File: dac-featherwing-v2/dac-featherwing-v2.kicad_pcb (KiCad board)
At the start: 2 copper layers, 22.9 x 50.7 mm, 15 parts, among them J1 BOT, J2 TOP, J3 35RASMT4BHNTRX, U1 WM1824CGEFL, U2 TLV320AIC3104IRHBR

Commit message: Dac featherwing schematic v2
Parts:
- removed U2: TLV320AIC3104IRHBR, Footprints:IC_ADS125H01IRHBT

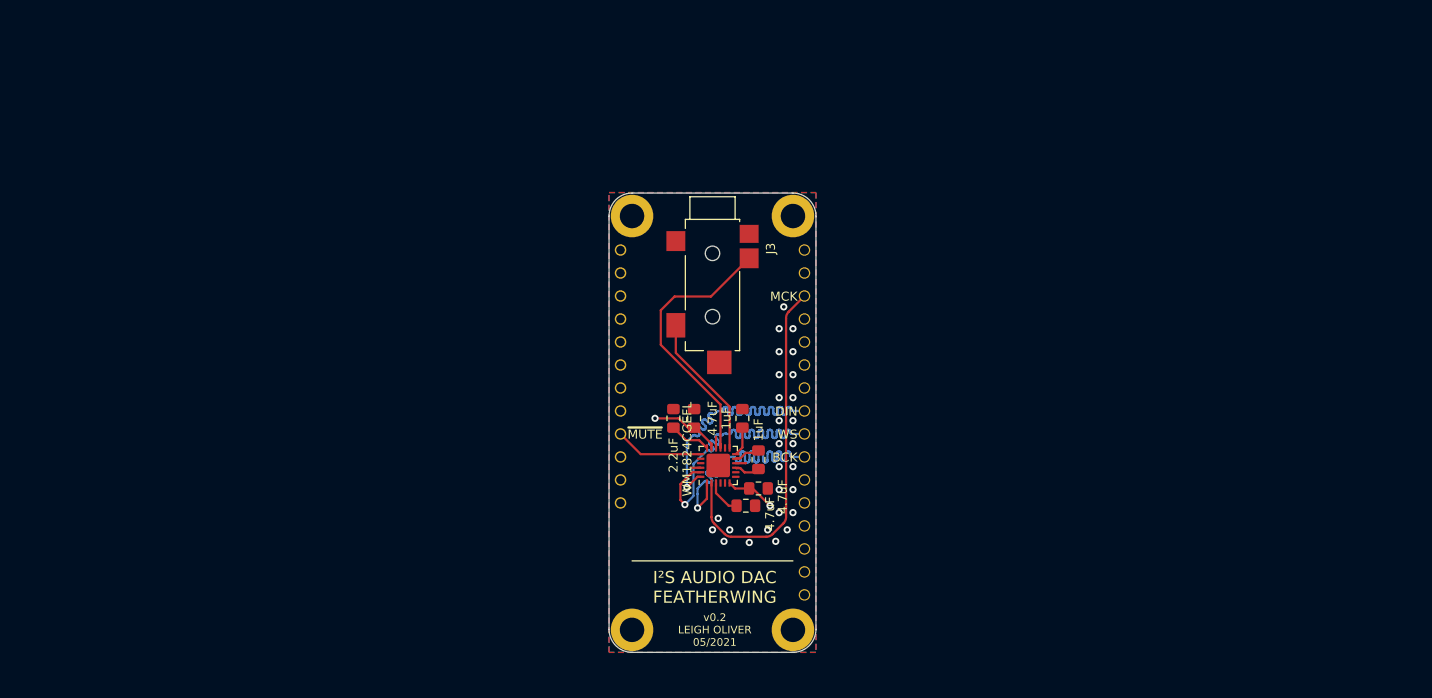
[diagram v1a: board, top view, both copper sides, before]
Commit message: Work on DAC Featherwing v2
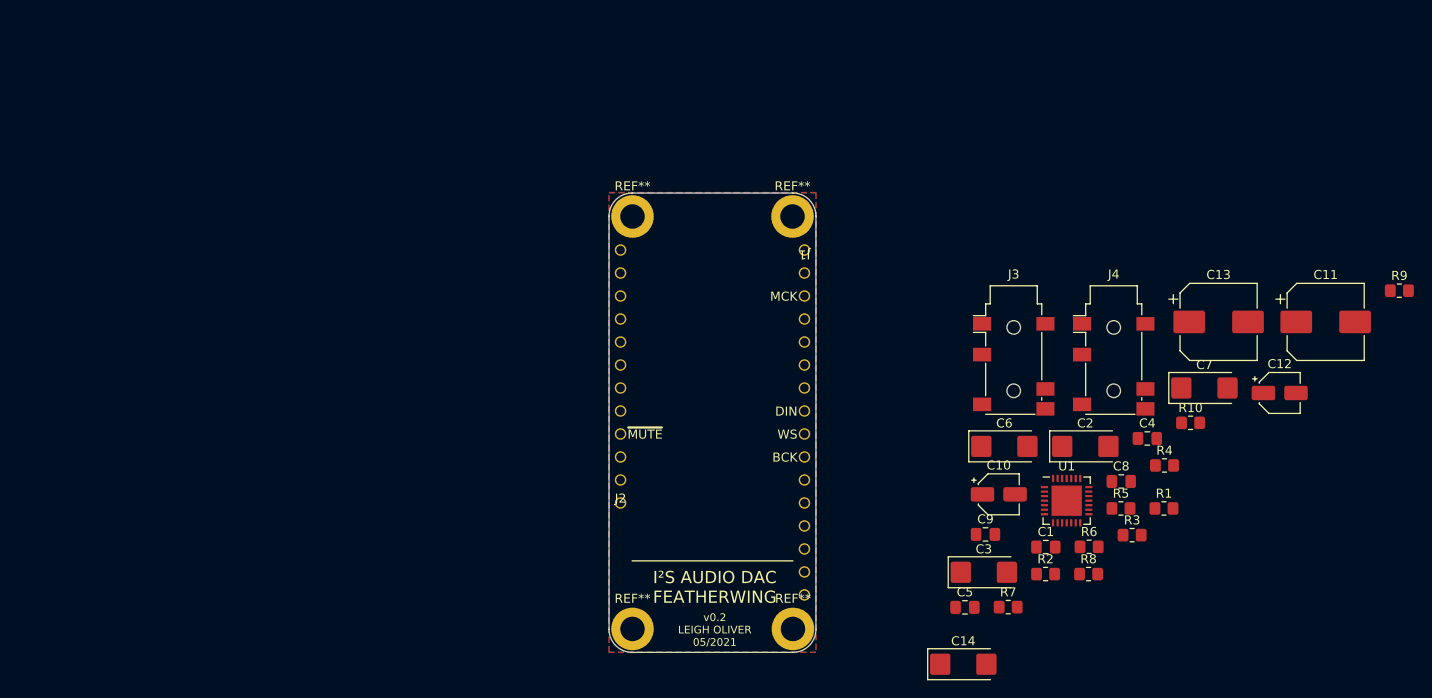
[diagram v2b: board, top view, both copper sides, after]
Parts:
- removed the REF** at (157.5, 75.2)
- removed the REF** at (175.3, 120.9)
- removed the REF** at (157.5, 120.9)
- removed the REF** at (175.3, 75.2)
- added C10: 1uF, Capacitor_SMD:CP_Elec_4x4.5, F.Cu at (198.0, 105.9)
- added C11: 220uF, Capacitor_SMD:CP_Elec_8x10, F.Cu at (234.1, 86.9)
- added C12: 1uF, Capacitor_SMD:CP_Elec_4x4.5, F.Cu at (229.0, 94.7)
- added C13: 220uF, Capacitor_SMD:CP_Elec_8x10, F.Cu at (222.3, 86.9)
- added C14: 10uF, Capacitor_Tantalum_SMD:CP_EIA-6032-20_AVX-F_Pad2.25x2.35mm_HandSolder, F.Cu at (194.1, 124.7)
- added C7: 10uF, Capacitor_Tantalum_SMD:CP_EIA-6032-20_AVX-F_Pad2.25x2.35mm_HandSolder, F.Cu at (220.7, 94.2)
- added C8: 0.1uF, Capacitor_SMD:C_0805_2012Metric_Pad1.18x1.45mm_HandSolder, F.Cu at (211.5, 104.5)
- added C9: 0.1uF, Capacitor_SMD:C_0805_2012Metric_Pad1.18x1.45mm_HandSolder, F.Cu at (196.5, 110.4)
- added J4: AudioJack4, Connector_Audio:Jack_3.5mm_PJ311_Horizontal, F.Cu at (210.7, 91.8)
- added R1: 4.7K, Resistor_SMD:R_0805_2012Metric_Pad1.20x1.40mm_HandSolder, F.Cu at (216.2, 107.5)
- added R10: 100, Resistor_SMD:R_0805_2012Metric_Pad1.20x1.40mm_HandSolder, F.Cu at (219.2, 98.0)
- added R2: 4.7K, Resistor_SMD:R_0805_2012Metric_Pad1.20x1.40mm_HandSolder, F.Cu at (203.2, 114.7)
- added R3: 10K, Resistor_SMD:R_0805_2012Metric_Pad1.20x1.40mm_HandSolder, F.Cu at (212.7, 110.4)
- added R4: 100, Resistor_SMD:R_0805_2012Metric_Pad1.20x1.40mm_HandSolder, F.Cu at (216.3, 102.7)
- added R5: 47K, Resistor_SMD:R_0805_2012Metric_Pad1.20x1.40mm_HandSolder, F.Cu at (211.5, 107.5)
- added R6: 47K, Resistor_SMD:R_0805_2012Metric_Pad1.20x1.40mm_HandSolder, F.Cu at (208.0, 111.7)
- added R7: 47K, Resistor_SMD:R_0805_2012Metric_Pad1.20x1.40mm_HandSolder, F.Cu at (199.0, 118.4)
- added R8: 47K, Resistor_SMD:R_0805_2012Metric_Pad1.20x1.40mm_HandSolder, F.Cu at (207.9, 114.7)
- added R9: 100, Resistor_SMD:R_0805_2012Metric_Pad1.20x1.40mm_HandSolder, F.Cu at (242.3, 83.4)
- added REF**: MountingHole_2.7mm_M2.5_DIN965_Pad, MountingHole:MountingHole_2.7mm_M2.5_DIN965_Pad, F.Cu at (157.5, 75.2)
- added REF**: MountingHole_2.7mm_M2.5_DIN965_Pad, MountingHole:MountingHole_2.7mm_M2.5_DIN965_Pad, F.Cu at (175.2, 75.2)
- added REF**: MountingHole_2.7mm_M2.5_DIN965_Pad, MountingHole:MountingHole_2.7mm_M2.5_DIN965_Pad, F.Cu at (157.5, 120.8)
- added REF**: MountingHole_2.7mm_M2.5_DIN965_Pad, MountingHole:MountingHole_2.7mm_M2.5_DIN965_Pad, F.Cu at (175.3, 120.8)
- C1, C5: value 4.7uF -> 0.1uF; footprint Capacitor_SMD:C_0805_2012Metric_Pad1.15x1.40mm_HandSolder -> Capacitor_SMD:C_0805_2012Metric_Pad1.18x1.45mm_HandSolder
- C2: value 4.7uF -> 10uF; footprint Capacitor_SMD:C_0805_2012Metric_Pad1.15x1.40mm_HandSolder -> Capacitor_Tantalum_SMD:CP_EIA-6032-20_AVX-F_Pad2.25x2.35mm_HandSolder
- C3: value 1uF -> 10uF; footprint Capacitor_SMD:C_0805_2012Metric_Pad1.15x1.40mm_HandSolder -> Capacitor_Tantalum_SMD:CP_EIA-6032-20_AVX-F_Pad2.25x2.35mm_HandSolder
- C4: value 1uF -> 0.1uF; footprint Capacitor_SMD:C_0805_2012Metric_Pad1.15x1.40mm_HandSolder -> Capacitor_SMD:C_0805_2012Metric_Pad1.18x1.45mm_HandSolder
- C6: value 2.2uF -> 10uF; footprint Capacitor_SMD:C_0805_2012Metric_Pad1.15x1.40mm_HandSolder -> Capacitor_Tantalum_SMD:CP_EIA-6032-20_AVX-F_Pad2.25x2.35mm_HandSolder
- J3: value 35RASMT4BHNTRX -> AudioJack4; footprint Footprints:SWITCHCRAFT_35RASMT4BHNTRX -> Connector_Audio:Jack_3.5mm_PJ311_Horizontal
- U1: value WM1824CGEFL -> WM8731CLSEFL; footprint Package_DFN_QFN:QFN-24-1EP_4x4mm_P0.5mm_EP2.6x2.6mm -> Package_DFN_QFN:QFN-28-1EP_5x5mm_P0.5mm_EP3.35x3.35mm
- moved C4 44.8 mm to (214.4, 99.8), turned to 0 degrees
- moved U1 38.7 mm to (205.5, 106.6), turned to 0 degrees
- moved C6 36.7 mm to (198.6, 100.6), turned to 0 degrees
- moved C5 36.5 mm to (194.3, 118.4), turned to 0 degrees
- moved C2 36.4 mm to (207.6, 100.6)
- moved J3 34.5 mm to (199.7, 91.8), turned to 0 degrees
- moved C1 33.5 mm to (203.2, 111.8)
- moved C3 27.8 mm to (196.3, 114.5), turned to 0 degrees
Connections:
- C1 pad 1: Net-(C1-Pad1) -> +3V3
- C3 pad 1: Net-(C3-Pad1) -> +3V3
- C3 pad 2: Net-(C3-Pad2) -> GND
- C4 pad 1: Net-(C4-Pad1) -> +3V3
- C5 pad 1: +3V3 -> +3.3VA
- C6 pad 1: Net-(C6-Pad1) -> +3.3VA
- J1 pad 3: /U1RXD/CLK_OUT3 -> /I2S_MCLK
- J3 pad 1: GND -> (no net)
- J3 pad 2: /OUTL -> (no net)
- J3 pad 3: /OUTR -> (no net)
- J3 pad 4: unconnected-(J3-Pad4) -> (no net)
- J3 pad 5: unconnected-(J3-Pad5) -> (no net)
- U1 pad 1: /I2S_BCK -> /I2S_MCLK
- U1 pad 10: GND -> unconnected-(U1-Pad10)
- U1 pad 11: Net-(C3-Pad2) -> unconnected-(U1-Pad11)
- U1 pad 12: Net-(C4-Pad1) -> +3.3VA
- U1 pad 13: /OUTR -> Net-(C11-Pad1)
- U1 pad 14: unconnected-(U1-Pad14) -> Net-(C13-Pad1)
- U1 pad 15: /OUTL -> GND
- U1 pad 16: GND -> Net-(C10-Pad1)
- U1 pad 17: +3V3 -> Net-(C12-Pad1)
- U1 pad 18: Net-(C6-Pad1) -> +3.3VA
- U1 pad 19: /~MUTE -> GND
- U1 pad 20: unconnected-(U1-Pad20) -> Net-(C14-Pad1)
- U1 pad 22: GND -> unconnected-(U1-Pad22)
- U1 pad 23: /I2S_WS -> unconnected-(U1-Pad23)
- U1 pad 24: /I2S_DO -> unconnected-(U1-Pad24)
- U1 pad 25: (no net) -> Net-(R3-Pad1)
- U1 pad 3: Net-(C1-Pad1) -> +3V3
- U1 pad 4: unconnected-(U1-Pad4) -> GND
- U1 pad 5: unconnected-(U1-Pad5) -> +3V3
- U1 pad 6: +3V3 -> Net-(R4-Pad2)
- U1 pad 7: unconnected-(U1-Pad7) -> /I2S_BCK
- U1 pad 8: unconnected-(U1-Pad8) -> /I2S_DO
- U1 pad 9: Net-(C3-Pad1) -> /I2S_WS
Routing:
- net unconnected-(U1-Pad2): track 39.3 -> 0.00 mm
- net /I2S_DO: track 35.5 -> 0.00 mm, vias 1 -> 0
- net /I2S_WS: track 35.4 -> 0.00 mm, vias 1 -> 0
- net /I2S_BCK: track 35.4 -> 0.00 mm, vias 1 -> 0
- net /OUTL: track 30.5 -> 0.00 mm
- net /OUTR: track 16.0 -> 0.00 mm
- net +3V3: track 13.4 -> 0.00 mm, vias 2 -> 0
- net /~MUTE: track 9.78 -> 0.00 mm
- net Net-(C6-Pad1): track 4.63 -> 0.00 mm
- net Net-(C1-Pad1): track 3.96 -> 0.00 mm
- net GND: track 3.47 -> 0.00 mm, vias 28 -> 0
- net Net-(C4-Pad1): track 3.23 -> 0.00 mm
- net Net-(C3-Pad2): track 2.88 -> 0.00 mm
- net Net-(C3-Pad1): track 2.87 -> 0.00 mm

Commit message: Capacitors checked. TRRS pins checked. 3.5mm Footprint made. Performing layout and routing.
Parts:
- removed R4: 100, Resistor_SMD:R_0805_2012Metric_Pad1.20x1.40mm_HandSolder
- removed the REF** at (157.5, 75.2)
- removed the REF** at (175.2, 75.2)
- removed the REF** at (157.5, 120.8)
- removed the REF** at (175.3, 120.8)
- added REF**: MountingHole_2.7mm_M2.5_DIN965_Pad, MountingHole:MountingHole_2.7mm_M2.5_DIN965_Pad, F.Cu at (132.1, 109.2)
- added REF**: MountingHole_2.7mm_M2.5_DIN965_Pad, MountingHole:MountingHole_2.7mm_M2.5_DIN965_Pad, F.Cu at (92.7, 55.9)
- added REF**: MountingHole_2.7mm_M2.5_DIN965_Pad, MountingHole:MountingHole_2.7mm_M2.5_DIN965_Pad, F.Cu at (132.1, 55.9)
- added REF**: MountingHole_2.7mm_M2.5_DIN965_Pad, MountingHole:MountingHole_2.7mm_M2.5_DIN965_Pad, F.Cu at (132.1, 63.5)
- added REF**: MountingHole_2.7mm_M2.5_DIN965_Pad, MountingHole:MountingHole_2.7mm_M2.5_DIN965_Pad, F.Cu at (92.7, 109.2)
- added REF**: MountingHole_2.7mm_M2.5_DIN965_Pad, MountingHole:MountingHole_2.7mm_M2.5_DIN965_Pad, F.Cu at (114.3, 109.2)
- added REF**: MountingHole_2.7mm_M2.5_DIN965_Pad, MountingHole:MountingHole_2.7mm_M2.5_DIN965_Pad, F.Cu at (114.3, 63.5)
- added REF**: MountingHole_2.7mm_M2.5_DIN965_Pad, MountingHole:MountingHole_2.7mm_M2.5_DIN965_Pad, F.Cu at (114.3, 55.9)
- C2, C3: footprint Capacitor_Tantalum_SMD:CP_EIA-6032-20_AVX-F_Pad2.25x2.35mm_HandSolder -> Capacitor_SMD:C_0805_2012Metric_Pad1.18x1.45mm_HandSolder
- C5, C6, C7, C8, R1, R2, R3: moved to B.Cu
- J3, J4: footprint Connector_Audio:Jack_3.5mm_PJ311_Horizontal -> Footprints:Lumberg 1503 20 VP3
- moved C11 138.3 mm to (95.9, 84.2), turned to 90 degrees
- moved R9 122.0 mm to (120.7, 73.8), turned to 90 degrees
- moved R5 118.4 mm to (97.4, 75.9), turned to 180 degrees
- moved C13 116.3 mm to (106.0, 84.2), turned to 90 degrees
- moved R6 109.6 mm to (104.4, 75.9), turned to 180 degrees
- moved C12 103.2 mm to (127.0, 79.5), turned to 90 degrees
- moved J3 101.8 mm to (101.0, 66.8), turned to 90 degrees
- moved C7 96.8 mm to (124.0, 91.9)
- moved R10 96.6 mm to (125.7, 73.8), turned to 90 degrees
- moved R7 94.1 mm to (116.2, 73.8), turned to -90 degrees
- moved J4 91.0 mm to (123.2, 66.8), turned to 90 degrees
- moved C8 88.1 mm to (124.0, 95.0)
- moved R8 87.9 mm to (130.2, 73.8), turned to 90 degrees
- moved R1 87.9 mm to (128.5, 102.6), turned to 180 degrees
- moved R3 86.0 mm to (127.5, 99.1), turned to 90 degrees
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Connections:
- C11 pad 2: LHPOUT -> RHPOUT
- C13 pad 2: RHPOUT -> LHPOUT
- R5 pad 2: LHPOUT -> RHPOUT
- R6 pad 1: RHPOUT -> LHPOUT
- U1 pad 13: Net-(C11-Pad1) -> Net-(C13-Pad1)
- U1 pad 14: Net-(C13-Pad1) -> Net-(C11-Pad1)
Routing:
- net Net-(C11-Pad1): track 0.00 -> 36.1 mm
- net RHPOUT: track 0.00 -> 27.4 mm
- net Net-(C13-Pad1): track 0.00 -> 25.5 mm
- net /I2S_DO: track 0.00 -> 23.0 mm
- net /I2S_WS: track 0.00 -> 22.9 mm
- net /I2S_BCK: track 0.00 -> 22.8 mm
- net LHPOUT: track 0.00 -> 19.0 mm
- net ROUT: track 0.00 -> 12.6 mm
- net Net-(C10-Pad2): track 0.00 -> 7.89 mm
- net Net-(C12-Pad2): track 0.00 -> 7.89 mm
- net LOUT: track 0.00 -> 5.29 mm
- added copper zone on B.Cu, net +3.3VA
- added copper zone on B.Cu, net GND
- removed copper zone on B.Cu, net +3V3
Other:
- board size 22.9 x 50.7 mm -> 44.5 x 58.4 mm
- board text added: "+BAT"
- board text added: "3V3"
- board text added: "GND"
- board text added: "VBUS"
- board text added: "v0.3 LEIGH OLIVER 06/2021"
- board text removed: "I²S AUDIO DAC FEATHERWING"
- board text removed: "v0.2 LEIGH OLIVER 05/2021"
- board text removed: "~MUTE"

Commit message: PCB changed
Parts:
- moved C9 4.70 mm to (125.0, 105.3)
- moved C14 1.52 mm to (123.4, 108.2)
- moved C1 1.44 mm to (129.0, 96.0)
- moved C2 0.25 mm to (130.3, 93.0)
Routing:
- net /I2S_MCLK: track 0.00 -> 29.0 mm, vias 0 -> 1
- net +3V3: track 0.00 -> 23.1 mm
- net GND: track 0.00 -> 10.8 mm
- net Net-(C14-Pad1): track 0.00 -> 5.94 mm
- net +3.3VA: track 0.00 -> 2.24 mm, vias 0 -> 2
- net Net-(R3-Pad1): track 0.00 -> 1.97 mm, vias 0 -> 1
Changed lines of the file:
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@@
   )
   (footprint "Capacitor_Tantalum_SMD:CP_EIA-6032-20_AVX-F_Pad2.25x2.35mm_HandSolder" (layer "F.Cu")
-    (at 123.444 106.68 180)
+    (at 123.444 108.204 180)
     (descr "Tantalum Capacitor SMD AVX-F (6032-20 Metric), IPC_7351 nominal, (Body size from: http://www.kemet.com/Lists/ProductCatalog/Attachments/253/KEM_TC101_STD.pdf), generated with kicad-footprint-generator")
     (tags "capacitor tantalum")
@@
   )
   (footprint "Capacitor_SMD:C_0805_2012Metric_Pad1.18x1.45mm_HandSolder" (layer "F.Cu")
-    (at 130.048 92.964)
+    (at 130.302 92.964)
     (descr "Capacitor SMD 0805 (2012 Metric), square (rectangular) end terminal, IPC_7351 nominal with elongated pad for handsoldering. (Body size source: IPC-SM-782 page 76, https://www.pcb-3d.com/wordpress/wp-content/uploads/ipc-sm-782a_amendment_1_and_2.pdf, https://docs.google.com/spreadsheets/d/1BsfQQcO9C6DZCsRaXUlFlo91Tg2WpOkGARC1WS5S8t0/edit?usp=sharing), generated with kicad-footprint-generator")
     (tags "capacitor handsolder")
@@
   )
   (footprint "Capacitor_SMD:C_0805_2012Metric_Pad1.18x1.45mm_HandSolder" (layer "F.Cu")
-    (at 123.444 109.728 180)
+    (at 124.968 105.283 180)
     (descr "Capacitor SMD 0805 (2012 Metric), square (rectangular) end terminal, IPC_7351 nominal with elongated pad for handsoldering. (Body size source: IPC-SM-782 page 76, https://www.pcb-3d.com/wordpress/wp-content/uploads/ipc-sm-782a_amendment_1_and_2.pdf, https://docs.google.com/spreadsheets/d/1BsfQQcO9C6DZCsRaXUlFlo91Tg2WpOkGARC1WS5S8t0/edit?usp=sharing), generated with kicad-footprint-generator")
     (tags "capacitor handsolder")
@@
   )
   (footprint "Capacitor_SMD:C_0805_2012Metric_Pad1.18x1.45mm_HandSolder" (layer "F.Cu")
-    (at 130.048 94.996)
+    (at 129.032 96.012)
     (descr "Capacitor SMD 0805 (2012 Metric), square (rectangular) end terminal, IPC_7351 nominal with elongated pad for handsoldering. (Body size source: IPC-SM-782 page 76, https://www.pcb-3d.com/wordpress/wp-content/uploads/ipc-sm-782a_amendment_1_and_2.pdf, https://docs.google.com/spreadsheets/d/1BsfQQcO9C6DZCsRaXUlFlo91Tg2WpOkGARC1WS5S8t0/edit?usp=sharing), generated with kicad-footprint-generator")
     (tags "capacitor handsolder")
@@
     (style (thickness 0.2) (arrow_length 1.27) (text_position_mode 0) (extension_height 0.58642) (extension_offset 0.5) keep_text_aligned)
   )
+  (segment (start 124.555 102.87) (end 124.555 103.8325) (width 0.25) (layer "F.Cu") (net 1))
+  (segment (start 124.555 103.8325) (end 126.0055 105.283) (width 0.25) (layer "F.Cu") (net 1))
+  (segment (start 126.0055 105.283) (end 125.994 105.2945) (width 1) (layer "F.Cu") (net 1))
+  (segment (start 125.994 105.2945) (end 125.994 108.204) (width 1) (layer "F.Cu") (net 1))
+  (segment (start 123.555 102.87) (end 123.555 103.703964) (width 0.25) (layer "F.Cu") (net 15))
+  (segment (start 120.224 100.92) (end 119.888 100.584) (width 0.25) (layer "F.Cu") (net 15))
+  (segment (start 123.555 103.703964) (end 123.521806 103.737158) (width 0.25) (layer "F.Cu") (net 15))
+  (segment (start 121.105 100.92) (end 120.224 100.92) (width 0.25) (layer "F.Cu") (net 15))
+  (via (at 119.888 100.584) (size 0.8) (drill 0.4) (layers "F.Cu" "B.Cu") (net 15))
+  (via (at 123.521806 103.737158) (size 0.8) (drill 0.4) (layers "F.Cu" "B.Cu") (net 15))
   (segment (start 134.309511 88.090566) (end 134.309511 86.049511) (width 0.25) (layer "F.Cu") (net 21))
   (segment (start 123.686096 94.245904) (end 129.032 88.9) (width 0.25) (layer "F.Cu") (net 21))
@@
   (arc (start 124.197247 96.340983) (mid 124.409379 96.428851) (end 124.621511 96.340983) (width 0.25) (layer "F.Cu") (net 23))
   (arc (start 123.501299 96.069299) (mid 123.713431 95.981431) (end 123.925563 96.069299) (width 0.25) (layer "F.Cu") (net 23))
+  (segment (start 122.055 101.92) (end 123.555 100.42) (width 0.25) (layer "F.Cu") (net 26))
+  (segment (start 123.555 97.97) (end 123.555 100.42) (width 0.25) (layer "F.Cu") (net 26))
+  (segment (start 122.055 102.87) (end 122.055 101.92) (width 0.25) (layer "F.Cu") (net 26))
+  (segment (start 126.005 99.92) (end 124.055 99.92) (width 0.25) (layer "F.Cu") (net 26))
+  (segment (start 124.055 99.92) (end 123.555 100.42) (width 0.25) (layer "F.Cu") (net 26))
+  (segment (start 124.055 100.92) (end 123.555 100.42) (width 0.25) (layer "F.Cu") (net 26))
+  (segment (start 124.055 102.87) (end 124.055 100.92) (width 0.25) (layer "F.Cu") (net 26))
+  (segment (start 123.325118 97.24548) (end 124.29504 97.24548) (width 0.25) (layer "F.Cu") (net 28))
+  (segment (start 133.35 102.87) (end 130.8315 102.87) (width 1) (layer "F.Cu") (net 28))
+  (segment (start 130.556 100.6055) (end 130.556 102.5945) (width 1) (layer "F.Cu") (net 28))
+  (segment (start 127.9945 100.033) (end 127.9945 96.012) (width 1) (layer "F.Cu") (net 28))
+  (segment (start 130.8315 102.87) (end 130.556 102.5945) (width 1) (layer "F.Cu") (net 28))
+  (segment (start 123.055 97.515598) (end 123.325118 97.24548) (width 0.25) (layer "F.Cu") (net 28))
+  (segment (start 129.2645 92.964) (end 127.9945 94.234) (width 1) (layer "F.Cu") (net 28))
+  (segment (start 127.9945 96.012) (end 127.777989 95.795489) (width 0.25) (layer "F.Cu") (net 28))
+  (segment (start 130.556 102.5945) (end 127.9945 100.033) (width 1) (layer "F.Cu") (net 28))
+  (segment (start 124.694243 97.24548) (end 124.29504 97.24548) (width 0.25) (layer "F.Cu") (net 28))
+  (segment (start 127.777989 95.795489) (end 126.144234 95.795489) (width 0.25) (layer "F.Cu") (net 28))
+  (segment (start 126.144234 95.795489) (end 124.694243 97.24548) (width 0.25) (layer "F.Cu") (net 28))
+  (segment (start 124.055 97.48552) (end 124.055 97.97) (width 0.25) (layer "F.Cu") (net 28))
+  (segment (start 127.9945 94.234) (end 127.9945 96.012) (width 1) (layer "F.Cu") (net 28))
+  (segment (start 123.055 97.97) (end 123.055 97.515598) (width 0.25) (layer "F.Cu") (net 28))
+  (segment (start 124.29504 97.24548) (end 124.055 97.48552) (width 0.25) (layer "F.Cu") (net 28))
   (segment (start 116.205 74.787) (end 120.65 74.787) (width 1) (layer "F.Cu") (net 32))
   (segment (start 119.38 77.702) (end 119.38 76.057) (width 1) (layer "F.Cu") (net 32))
@@
   (segment (start 96.409 75.946) (end 95.065489 74.602489) (width 1) (layer "F.Cu") (net 36))
   (segment (start 95.065489 74.602489) (end 95.065489 66.242391) (width 1) (layer "F.Cu") (net 36))
+  (segment (start 125.055 97.957) (end 125.055 97.97) (width 0.25) (layer "F.Cu") (net 37))
+  (segment (start 126.492 96.52) (end 125.055 97.957) (width 0.25) (layer "F.Cu") (net 37))
+  (via (at 126.492 96.52) (size 0.8) (drill 0.4) (layers "F.Cu" "B.Cu") (net 37))
+  (segment (start 132.08 90.424) (end 132.08 73.66) (width 0.25) (layer "B.Cu") (net 37))
+  (segment (start 132.08 73.66) (end 133.35 72.39) (width 0.25) (layer "B.Cu") (net 37))
+  (segment (start 126.492 96.52) (end 126.492 96.012) (width 0.25) (layer "B.Cu") (net 37))
+  (segment (start 126.492 96.012) (end 132.08 90.424) (width 0.25) (layer "B.Cu") (net 37))
+  (segment (start 126.705258 100.42) (end 126.005 100.42) (width 0.25) (layer "F.Cu") (net 38))
+  (segment (start 127.601758 101.3165) (end 126.705258 100.42) (width 0.25) (layer "F.Cu") (net 38))
+  (via (at 127.601758 101.3165) (size 0.8) (drill 0.4) (layers "F.Cu" "B.Cu") (net 38))
   (segment (start 120.65 72.787) (end 120.65 69.212) (width 1) (layer "F.Cu") (net 40))
   (segment (start 120.65 69.212) (end 119.44 68.002) (width 1) (layer "F.Cu") (net 40))
